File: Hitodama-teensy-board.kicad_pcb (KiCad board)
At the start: 2 copper layers, 101.6 x 127 mm, 16 parts, among them J1 Jack-DC, J2 Conn_01x20_Female, J3 Conn_01x20_Female, J4 Conn_01x20_Female, U4 Teensy3.6

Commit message: trying different routing options teensy board
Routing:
- net VCC: track 0.00 -> 226.2 mm, vias 0 -> 2
- net /All.Stby: track 0.00 -> 209.2 mm, vias 0 -> 2
- net /ChamberC.PWM: track 0.00 -> 120.2 mm
- net /ChamberH.D2: track 0.00 -> 118.1 mm, vias 0 -> 1
- net /ChamberH.ADC: track 0.00 -> 114.6 mm, vias 0 -> 2
- net /ChamberI.D1: track 0.00 -> 98.5 mm, vias 0 -> 1
- net /ChamberC.D2: track 0.00 -> 97.9 mm
- net /ChamberG.PWM: track 0.00 -> 97.6 mm
- net /SPI0.SCK: track 0.00 -> 94.5 mm
- net /ChamberG.D3: track 0.00 -> 94.4 mm, vias 0 -> 1
- net /ChamberA.D1: track 0.00 -> 93.1 mm, vias 0 -> 2
- net GND: track 0.00 -> 91.8 mm, vias 0 -> 3
- net /ChamberA.D2: track 0.00 -> 91.5 mm, vias 0 -> 2
- net +12V: track 0.00 -> 88.6 mm
- net /SPI0.MISO: track 0.00 -> 86.5 mm
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
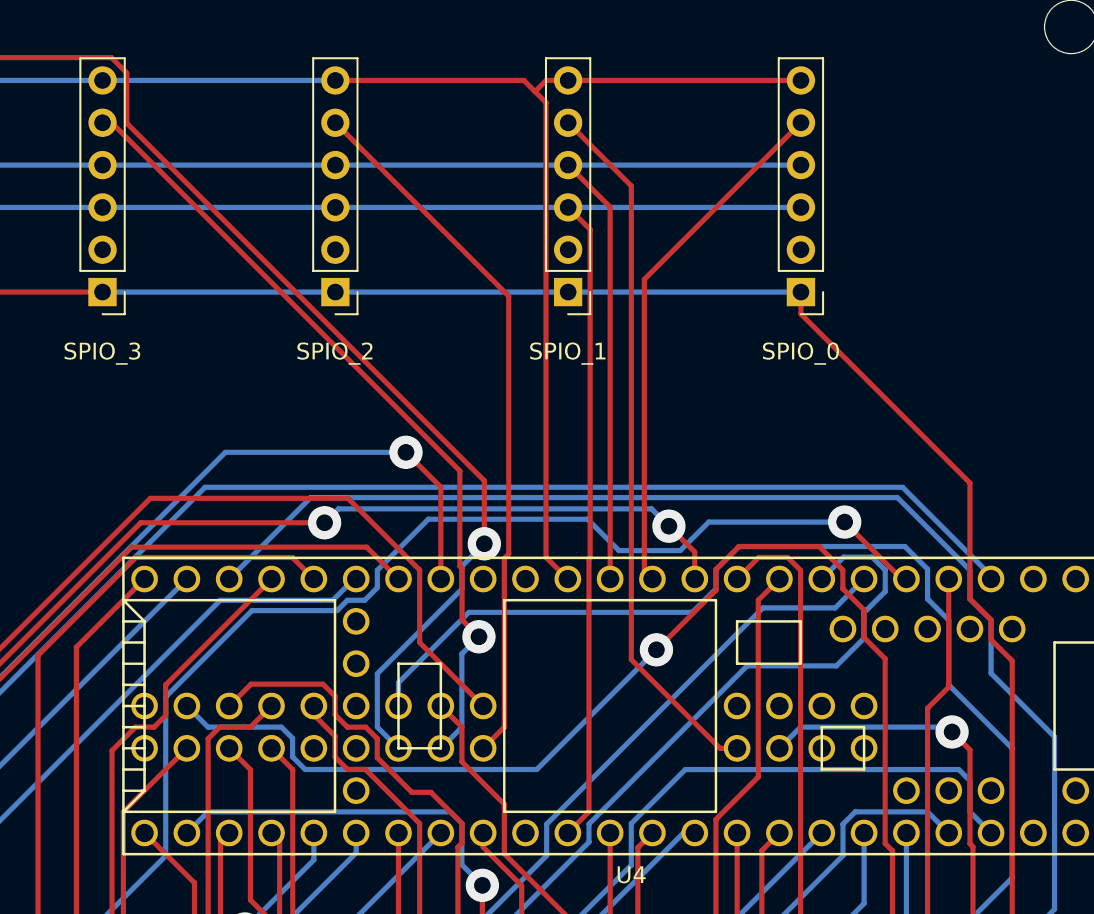
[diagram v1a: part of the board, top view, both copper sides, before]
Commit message: fix cap wrong orientation & teensy vcc.
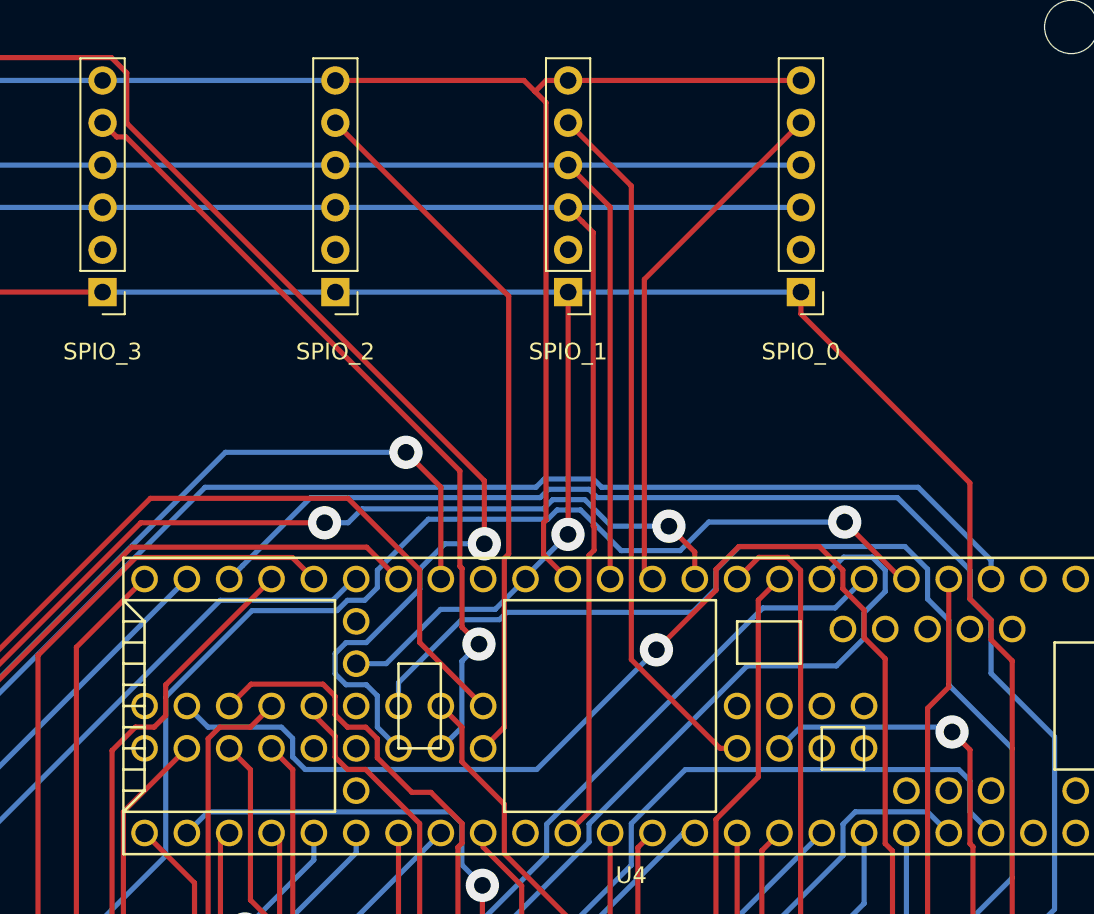
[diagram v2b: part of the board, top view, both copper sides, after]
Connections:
- U4 pad 15: +3V3 -> VCC
- U4 pad 26: Net-(U4-Pad26) -> VCC
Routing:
- net VCC: track 226.2 -> 256.7 mm, vias 2 -> 3
- net /SPI0.CS4: track 70.0 -> 74.9 mm
- net /ChamberC.PWM: track 120.2 -> 121.2 mm

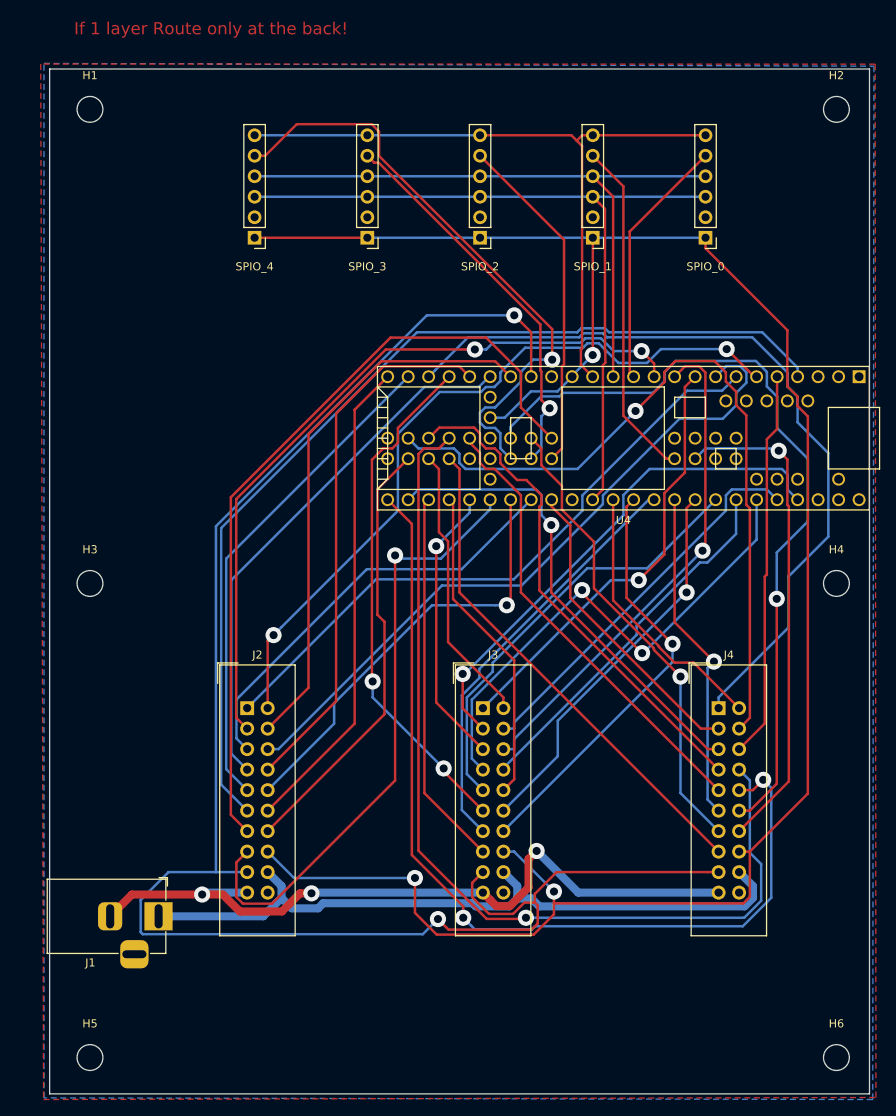
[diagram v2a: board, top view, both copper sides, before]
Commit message: reduce teensy board size to 100x100
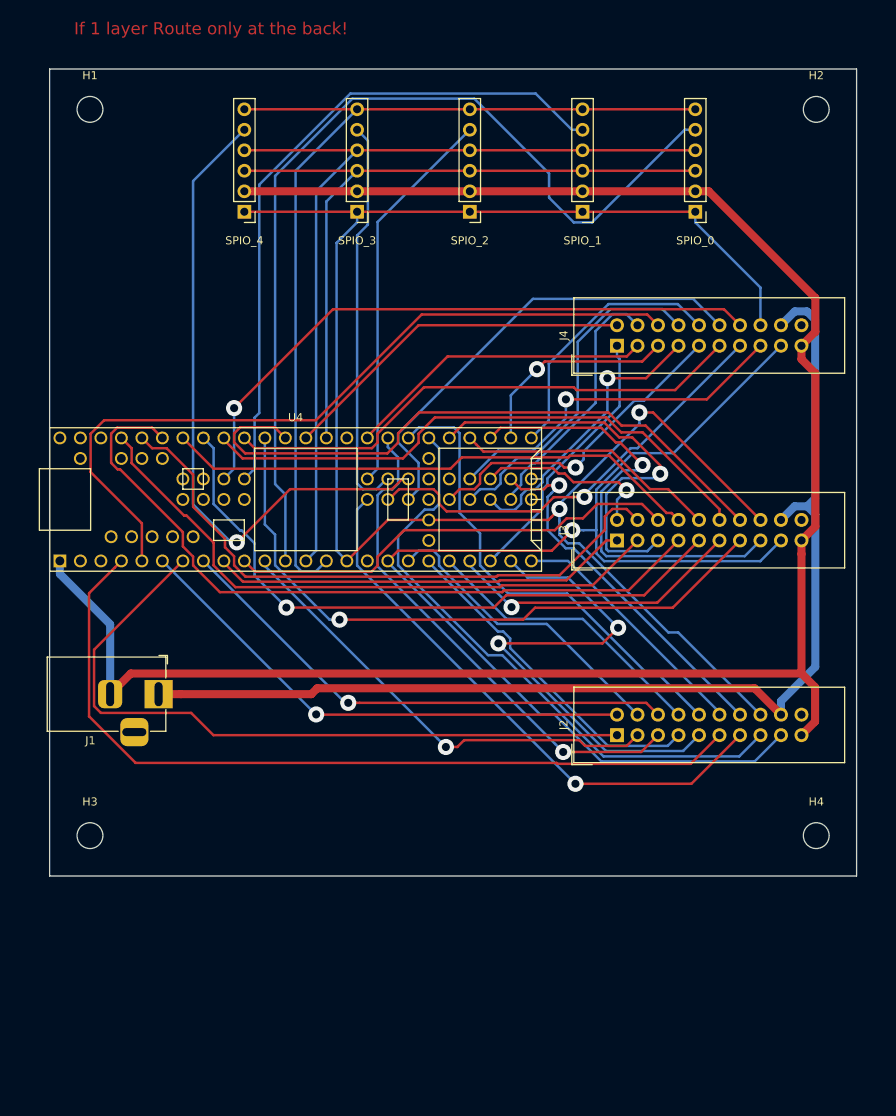
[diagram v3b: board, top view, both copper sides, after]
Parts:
- removed H5, H6: MountingHole, MountingHole:MountingHole_3.2mm_M3
- moved J4 46.6 mm to (70.3, 34.3), turned to 90 degrees
- moved J2 46.0 mm to (70.3, 82.5), turned to 90 degrees
- moved U4 41.3 mm to (30.5, 53.3), turned to 0 degrees
- moved H4 31.3 mm to (95.0, 95.0)
- moved H3 31.2 mm to (5.00, 95.0)
- moved J1 27.5 mm to (13.5, 77.5)
- moved J3 26.6 mm to (70.3, 58.4), turned to 90 degrees
- moved SPIO_2 3.46 mm to (52.1, 17.7)
- moved SPIO_4 3.46 mm to (24.1, 17.7)
- moved SPIO_0 3.46 mm to (80.0, 17.7)
- moved SPIO_1 3.46 mm to (66.0, 17.7)
- moved SPIO_3 3.46 mm to (38.1, 17.7)
- moved H2 2.50 mm to (95.0, 5.00)
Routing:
- net GND: track 91.8 -> 239.8 mm, vias 3 -> 0
- net /SPI0.CS0: track 31.5 -> 117.1 mm
- net /ChamberH.ADC: track 114.6 -> 32.9 mm, vias 2 -> 0
- net /ChamberH.D2: track 118.1 -> 42.3 mm, vias 1 -> 0
- net /ChamberG.PWM: track 98.0 -> 33.4 mm
- net /ChamberG.D3: track 94.4 -> 32.0 mm, vias 1 -> 0
- net /All.Stby: track 209.2 -> 150.4 mm, vias 2 -> 1
- net +12V: track 88.6 -> 139.6 mm
- net /ChamberH.PWM: track 48.1 -> 95.4 mm
- net /SPI0.CS1: track 42.3 -> 83.8 mm
- net /ChamberI.D1: track 98.5 -> 57.8 mm, vias 1 -> 0
- net VCC: track 256.7 -> 221.1 mm, vias 3 -> 2
- net /ChamberA.D2: track 92.0 -> 57.3 mm, vias 2 -> 1
- net /SPI0.MISO: track 86.6 -> 120.2 mm
- net /ChamberG.ADC: track 58.7 -> 26.1 mm
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- removed copper zone on B.Cu, net GND
- removed copper zone on F.Cu, net GND
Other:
- board size 101.6 x 127 mm -> 100 x 100 mm

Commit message: fix wrong adc pins in teensy board
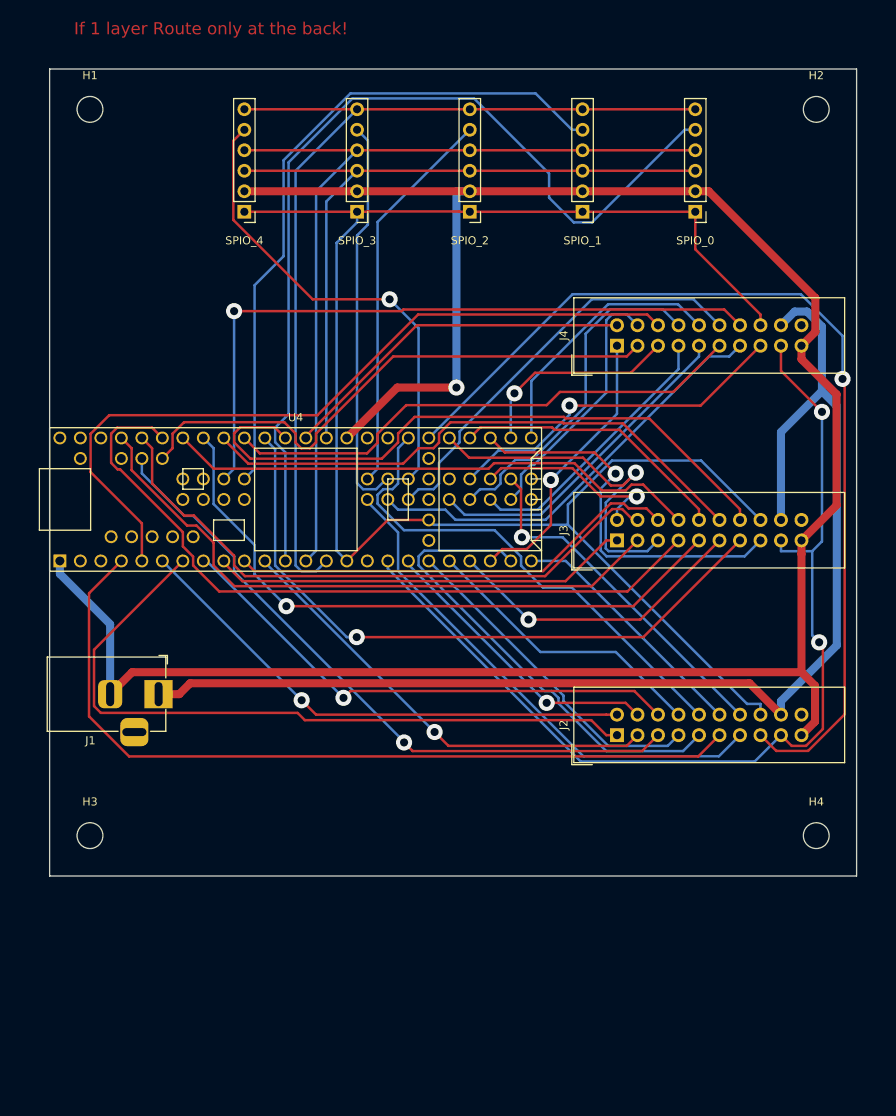
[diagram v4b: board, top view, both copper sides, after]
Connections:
- U4 pad 37: /ChamberA.ADC -> /A10
- U4 pad 38: /ChamberG.D2 -> /A11
- U4 pad 39: Net-(U4-Pad39) -> GND
- U4 pad 56: /A10 -> /ChamberA.ADC
- U4 pad 57: /A11 -> /ChamberG.D2
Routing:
- net /ChamberC.ADC: track 74.9 -> 120.9 mm, vias 0 -> 1
- net GND: track 239.8 -> 284.2 mm, vias 0 -> 1
- net /ChamberG.D2: track 38.3 -> 69.7 mm
- net /All.Stby: track 150.4 -> 123.4 mm, vias 1 -> 2
- net /SPI0.CS4: track 80.9 -> 59.5 mm
- net /ChamberA.ADC: track 63.3 -> 82.0 mm
- net +12V: track 139.6 -> 155.6 mm
- net /ChamberD.ADC: track 51.8 -> 44.3 mm
- net /ChamberF.ADC: track 56.0 -> 48.6 mm
- net VCC: track 221.1 -> 214.0 mm, vias 2 -> 0
- net /ChamberI.D3: track 77.9 -> 84.9 mm
- net /ChamberC.D2: track 69.9 -> 63.4 mm, vias 1 -> 0
- net /ChamberI.D1: track 57.8 -> 52.5 mm
- net /ChamberB.D3: track 63.6 -> 58.9 mm, vias 2 -> 0
- net /ChamberB.ADC: track 59.4 -> 61.7 mm
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
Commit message: added logos
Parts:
- added G***: LOGO, Hitodama_Logo:hitodama_vertical, F.Cu at (5.08, 24.1)
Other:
- board text removed: "If 1 layer Route only at the back!"

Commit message: Merge branch 'joaquin' into HEAD
# Conflicts:
#	Hitodama-teensy-board.kicad_pcb
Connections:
- U4 pad 51: Net-(U4-Pad51) -> VCC
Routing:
- net VCC: track 214.0 -> 249.4 mm
